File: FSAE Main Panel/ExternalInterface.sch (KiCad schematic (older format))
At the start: 46 parts, among them J201 USB Micro B, J203 Conn_01x08, J204 Conn, J3 Conn, J5 Cortex_Debug, J6 Conn, SW1 SW_SPST, SW2 SW_SPST, U201 CD40106BPWR, U202 CD74HC238PWR

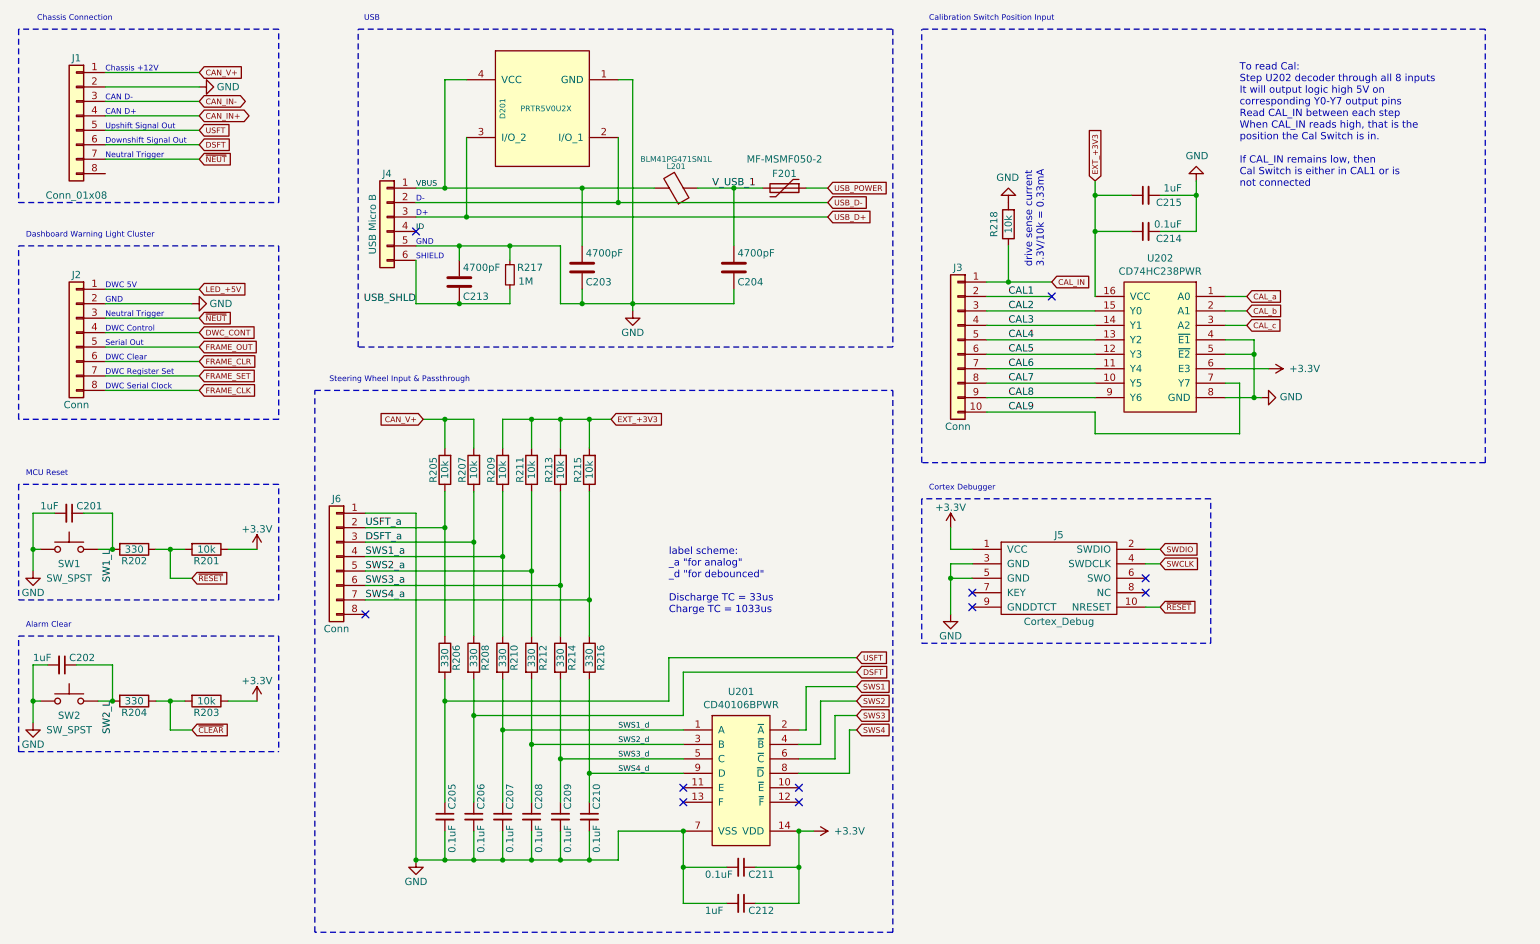
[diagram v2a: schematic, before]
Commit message: Completed Circuit and BOM
First finished draft of circuit design
Completed BOM
Footprints assigned
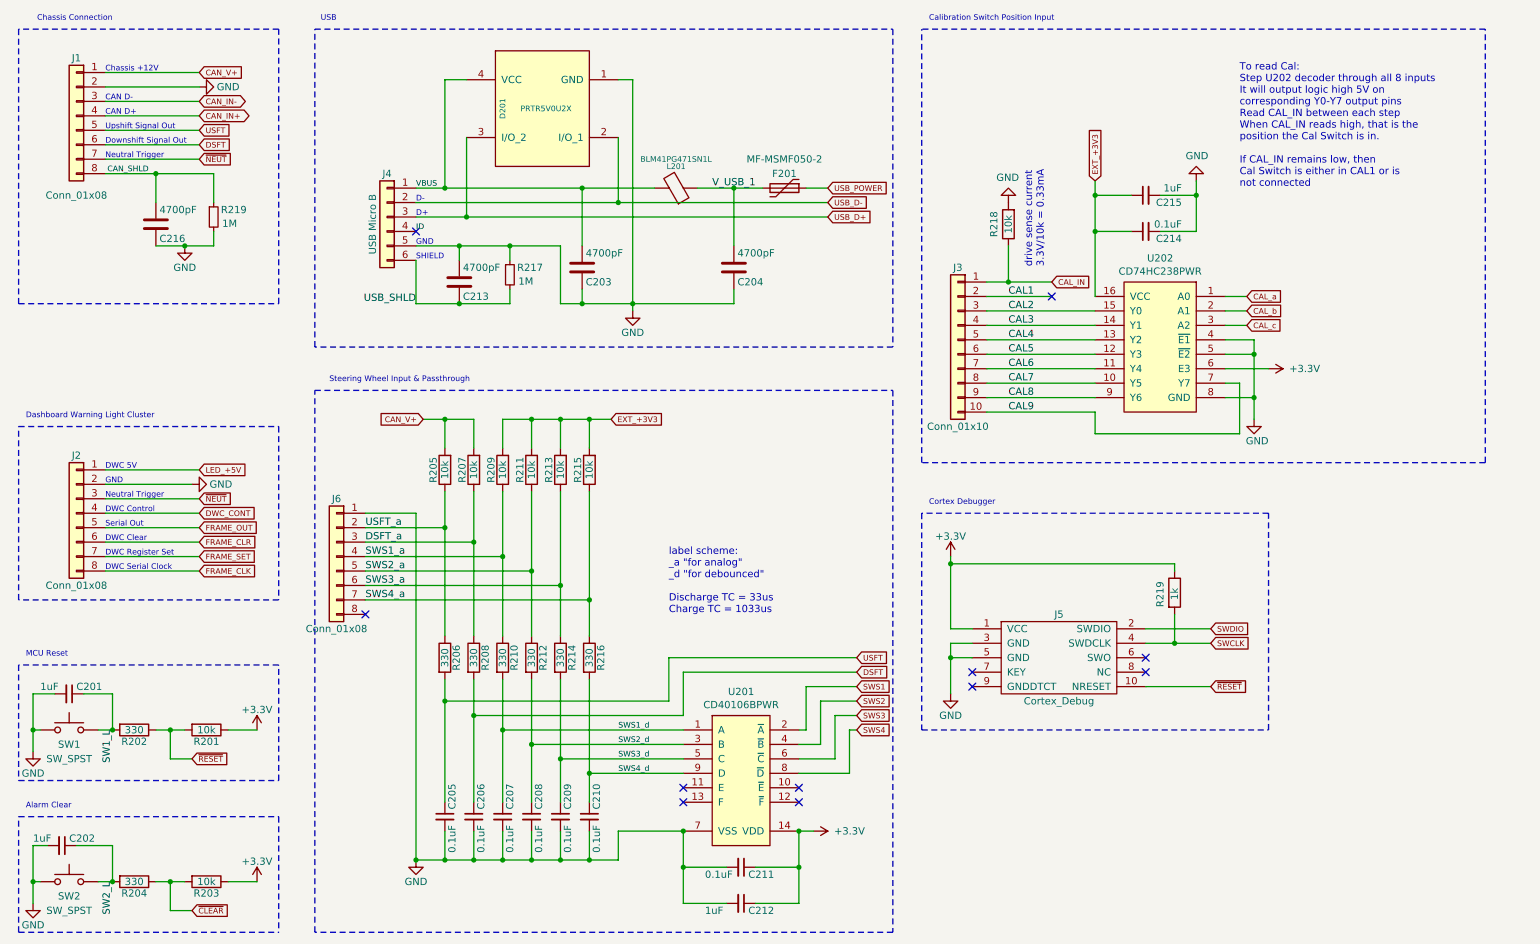
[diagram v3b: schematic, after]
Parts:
- added C216: 4700pF, Capacitors_SMD:C_0603, symbol Device:C
- added R219: 1k, Resistors_SMD:R_0603, symbol Device:R
- added R219: 1M, Resistors_SMD:R_0603, symbol Device:R_Small
- C201, C202: Description (none) -> CAP CER 0603 1UF 16V X7R 10%; Digikey P/N (none) -> 399-17704-1-ND; Part Number C0603C105K4RACTU -> C0603C105K4RACAUTO
- C203, C204, C213: Digikey P/N (none) -> 399-6896-1-ND; Part Number C0603C472K5RACTU -> C0603C472K5RACAUTO
- C205: Description (none) -> CAP CER 0.1UF 50V X7R 0603; Digikey P/N (none) -> 399-6856-1-ND; Part Number (none) -> C0603C104K5RACAUTO
- C206, C207, C208, C209, C210, C211, C214: Description (none) -> CAP CER 0.1UF 50V X7R 0603; Digikey P/N (none) -> 399-6856-1-ND; Manufacturer (none) -> KEMET; Part Number (none) -> C0603C104K5RACAUTO
- C212, C215: Description (none) -> CAP CER 0603 1UF 16V X7R 10%; Digikey P/N (none) -> 399-17704-1-ND; Manufacturer (none) -> KEMET; Part Number (none) -> C0603C105K4RACAUTO
- D201: Digikey P/N (none) -> 1727-3884-1-ND
- F201: Digikey P/N (none) -> IRLML6402PBFCT-ND
- J201: Description Micro USB -> CONN RCPT USB2.0 MICRO B SMD R/A; Digikey P/N (none) -> 609-4613-1-ND
- J203: footprint (none) -> Connectors_Molex:Molex_KK-6410-08_08x2.54mm_Straight; Description (none) -> CONN HEADER R/A 8POS 2.54MM; Digikey P/N (none) -> WM10303-ND; Manufacturer (none) -> Molex; Part Number (none) -> 1718571008
- J204, J6: value Conn -> Conn_01x08; Description (none) -> CONN HEADER R/A 8POS 2.54MM; Digikey P/N (none) -> WM10303-ND
- J3: value Conn -> Conn_01x10; footprint (none) -> Connectors_Molex:Molex_KK-6410-10_10x2.54mm_Straight; Description (none) -> CONN HEADER R/A 10POS 2.54MM; Digikey P/N (none) -> WM2719-ND; Manufacturer (none) -> Molex; Part Number (none) -> 0022122104
- J5: Description Cortex Debug -> CONN HEADER VERT 10POS 1.27MM; Digikey P/N (none) -> 609-3712-ND
- L201: Description 470 Ohm Ferrite Bead 1806 -> FERRITE BEAD 470 OHM 1806 1LN; Digikey P/N (none) -> 490-1060-1-ND; Manufacturer (none) -> Murata
- R201, R203, R205, R207, R209, R211, R213, R215, R218: Description (none) -> RES 10K OHM 5% 1/10W 0603; Digikey P/N (none) -> RMCF0603JT10K0CT-ND; Manufacturer (none) -> Stackpole; Part Number (none) -> RMCF0603JT10K0
- R202, R204, R206, R208, R210, R212, R214, R216: Description (none) -> RES 330 OHM 5% 1/10W 0603; Digikey P/N (none) -> RMCF0603JT330RCT-ND; Manufacturer (none) -> Stackpole; Part Number (none) -> RMCF0603JT330R
- R217: footprint (none) -> Resistors_SMD:R_0603; Description (none) -> RES 1M OHM 5% 1/10W 0603; Digikey P/N (none) -> RMCF0603JT1M00CT-ND; Manufacturer (none) -> Stackpole; Part Number (none) -> RMCF0603JT1M00
- U201: Description (none) -> Inverter IC 6 Channel Schmitt Trigger 14-TSSOP; Digikey P/N (none) -> 296-14082-1-ND; Manufacturer (none) -> TI; Part Number (none) -> CD40106BPWR
- U202: Description (none) -> Decoder/Demultiplexer 1 x 3:8 16-TSSOP; Digikey P/N (none) -> 296-13814-1-ND; Manufacturer (none) -> TI; Part Number (none) -> CD74HC238PWR
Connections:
- net +3V3: now also R219.1
- net GND: now also C216.1, R219.2
- net SWCLK: now also R219.2
- net CAN_SHLD: now reaches J203.8 (Pin_8)
- net CAN_SHLD: now also C216.2, R219.1
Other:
- moved on the sheet: C201, C202, J2, J5, R201, R202, R203, R204, SW1, SW2
